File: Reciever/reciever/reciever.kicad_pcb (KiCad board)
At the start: 2 copper layers, 24 parts, among them J1 USB_C_Receptacle_USB2.0_14P, J2 UART/I2C, J3 TWAI, SW1 Button, SW2 Button, U1 TXS0102DCU, U2 LM66200, U3 SE5218ALG-LF, U4 ESP32-C6-MINI-1, U5 TCAN330DR

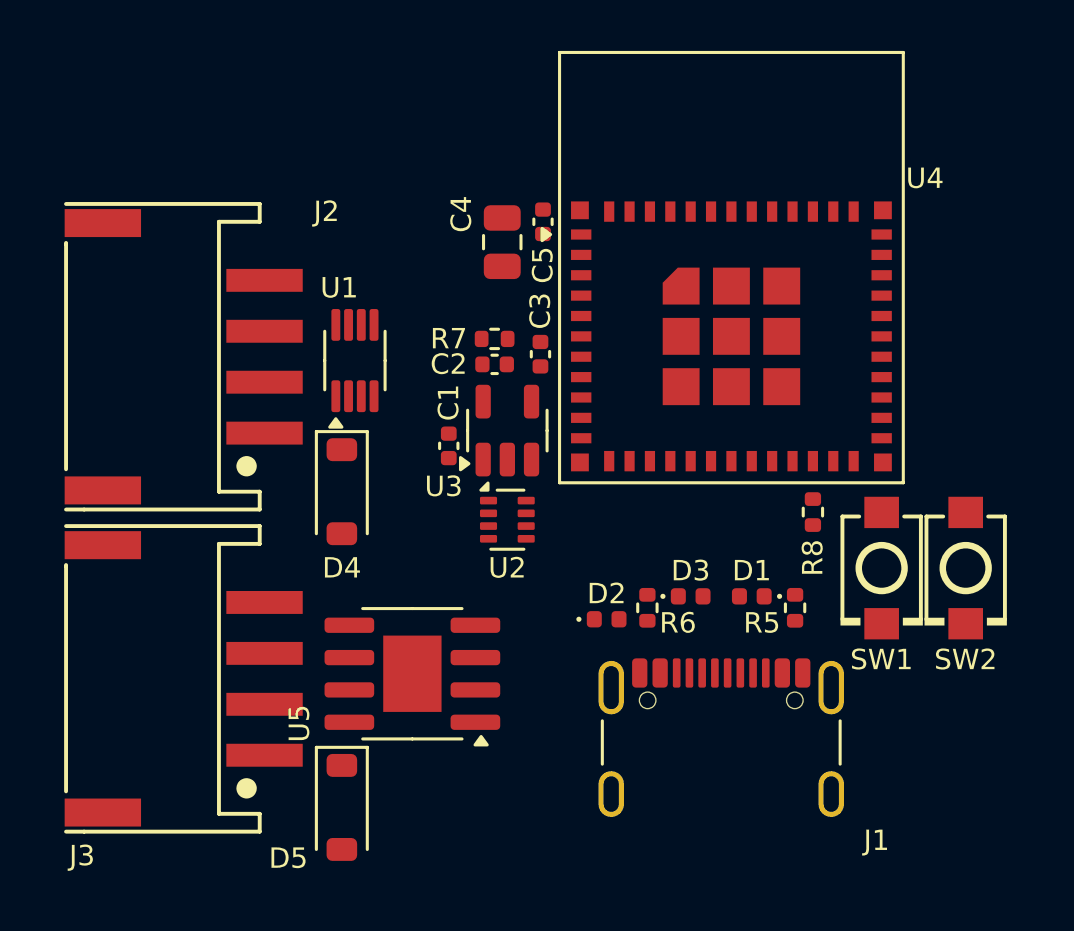
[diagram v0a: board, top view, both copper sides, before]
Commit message: crc v2
main board and receiver finalized. ready for assembly!
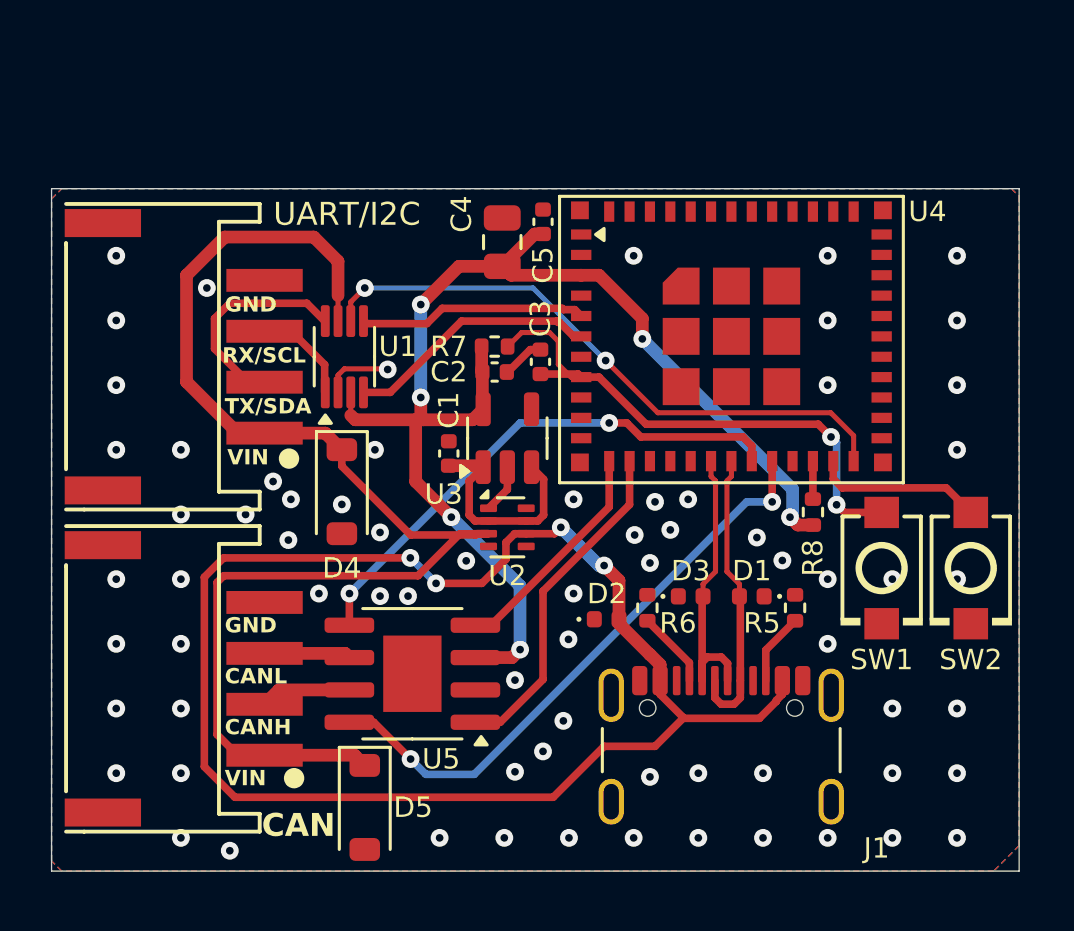
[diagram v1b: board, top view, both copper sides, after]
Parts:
- added G***: LOGO, LOGO, B.Cu at (145.0, 107.5)
- moved D5 0.90 mm to (138.0, 118.9)
- moved U1 0.44 mm to (137.2, 101.2)
- moved C3 0.30 mm to (144.9, 101.4)
- moved U2 0.30 mm to (143.6, 107.9)
- moved U3 0.30 mm to (143.6, 104.4)
- moved C1 0.30 mm to (141.3, 105.0)
- moved C2 0.30 mm to (143.1, 101.8)
- moved J1 0.30 mm to (152.0, 117.6)
- moved R7 0.30 mm to (143.1, 100.8)
- moved SW2 0.20 mm to (161.8, 109.5)
- renumbered J3 to CAN, J2 to UART/I2C
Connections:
- U4 pad 12: TWAITX -> TWAIRX
- U4 pad 13: TWAIRX -> TWAITX
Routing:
- net +USB5V: track 0.00 -> 59.3 mm, vias 0 -> 4
- net VIN: track 0.00 -> 52.0 mm
- net +3.3V: track 0.00 -> 49.9 mm, vias 0 -> 6
- net TRANS_EN: track 0.00 -> 24.1 mm, vias 0 -> 2
- net SILENT: track 0.00 -> 23.5 mm, vias 0 -> 2
- net /RESET: track 0.00 -> 21.5 mm, vias 0 -> 2
- net SHDN: track 0.00 -> 20.8 mm, vias 0 -> 2
- net TWAITX: track 0.00 -> 13.3 mm
- net USB_D-: track 0.00 -> 11.5 mm
- net USB_D+: track 0.00 -> 11.5 mm
- net UARTRX/SCL: track 0.00 -> 9.93 mm
- net TWAIRX: track 0.00 -> 8.98 mm
- net UARTTX/SDA: track 0.00 -> 8.94 mm
- net +5V: track 0.00 -> 8.68 mm
- net UARTTX/SDA_IN: track 0.00 -> 8.56 mm
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- added copper zone on B.Cu, net GND
- added copper zone on F.Cu, net GND
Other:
- board outline added: 38 x 26.8 mm
- board text added: "CANH"
- board text added: "CANL"
- board text added: "GND"
- board text added: "MATTHEW EMBAYE"
- board text added: "RX/SCL"
- board text added: "TX/SDA"
- board text added: "VIN"

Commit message: crc v2
remote and receiver complete! assembly and orders have been prepared for purchasing.
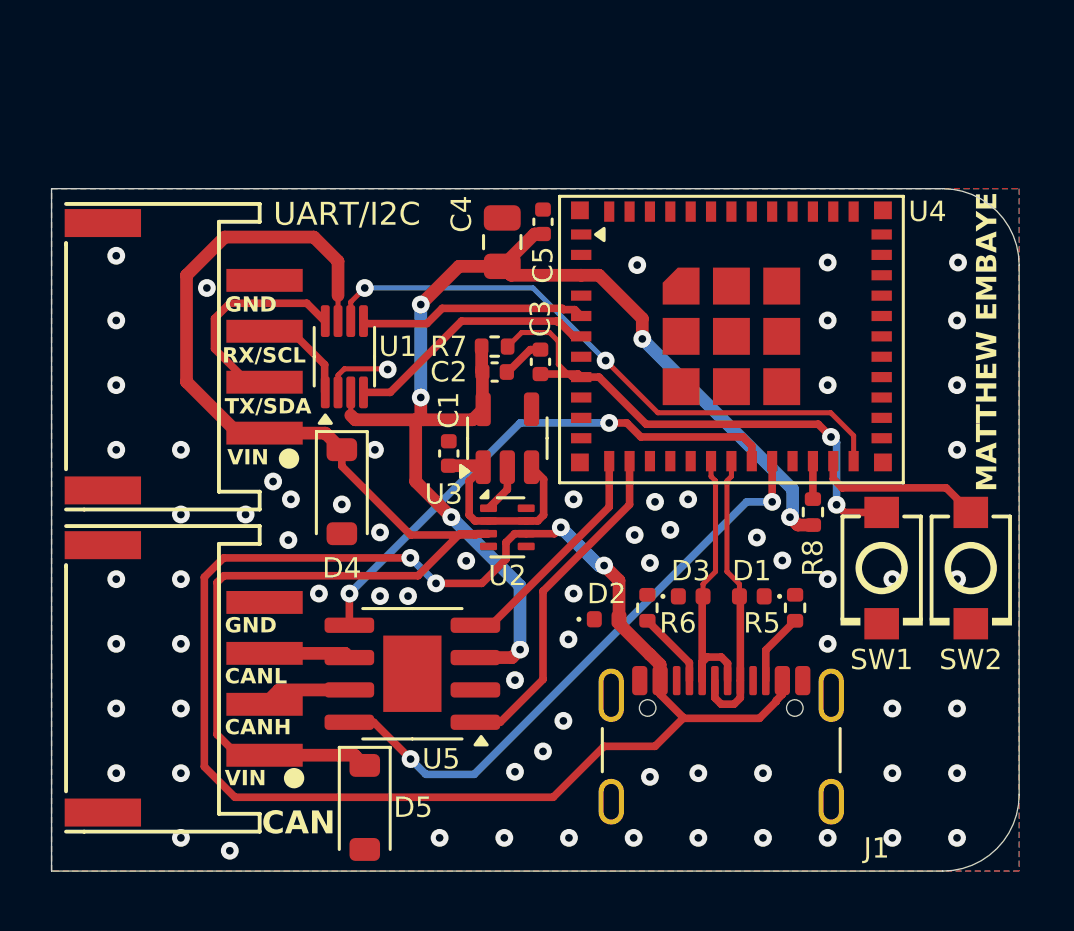
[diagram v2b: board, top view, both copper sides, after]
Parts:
- moved G*** 10.9 mm to (145.7, 96.6), turned to 0 degrees
- renumbered UART/I2C to J2, CAN to J3
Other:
- outline, holes or cut-outs redrawn
- board text added: "CAN"
- board text added: "UART/I2C"

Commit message: Custom RC V2
Final Remote + Receiver!

Special thanks to the CRCW25 Electrical Team who contributed to its development!

Jun
Katie
Nelson
David
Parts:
- D1, D2, D3: value 6V TVS -> 15V TVS
- D4, D5: value D_Schottky -> 15V TVS; footprint Diode_SMD:D_SOD-123 -> Diode_SMD:D_0402_1005Metric
- moved D5 13.8 mm to (136.6, 105.2), turned to 90 degrees
- moved D4 10.7 mm to (137.9, 117.2), turned to 180 degrees
- renumbered SW2 to FLASH, SW1 to RESET
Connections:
- D4 pad 1: VIN -> GND
- D4 pad 2: GND -> VIN
- D5 pad 1: VIN -> GND
- D5 pad 2: GND -> VIN
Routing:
- net VIN: track 52.0 -> 51.0 mm
